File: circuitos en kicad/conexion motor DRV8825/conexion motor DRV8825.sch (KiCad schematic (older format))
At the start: 29 parts, among them P1 CONN_3X2, P10 CONN_2, P2 CONN_2, P3 CONN_2, P4 CONN_2, P5 CONN_2, P6 CONN_2, P7 CONN_2, P8 CONN_2, P9 CONN_2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

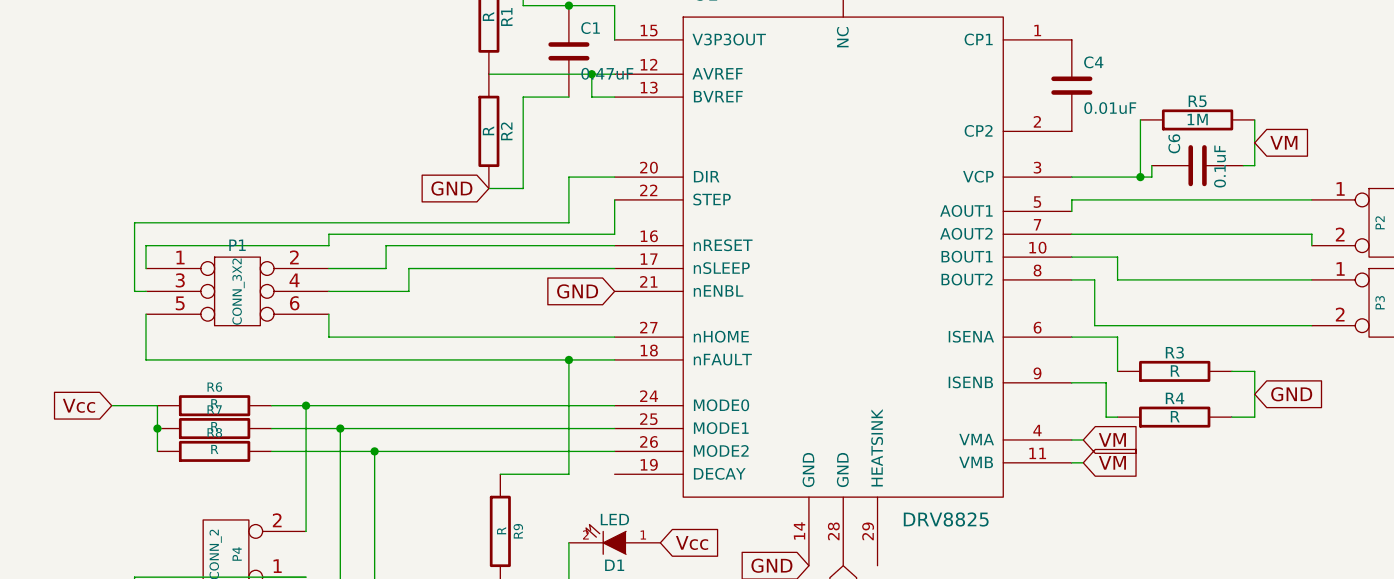
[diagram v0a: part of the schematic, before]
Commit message: Placa del DRV8825 actualizada al 25/07/2014
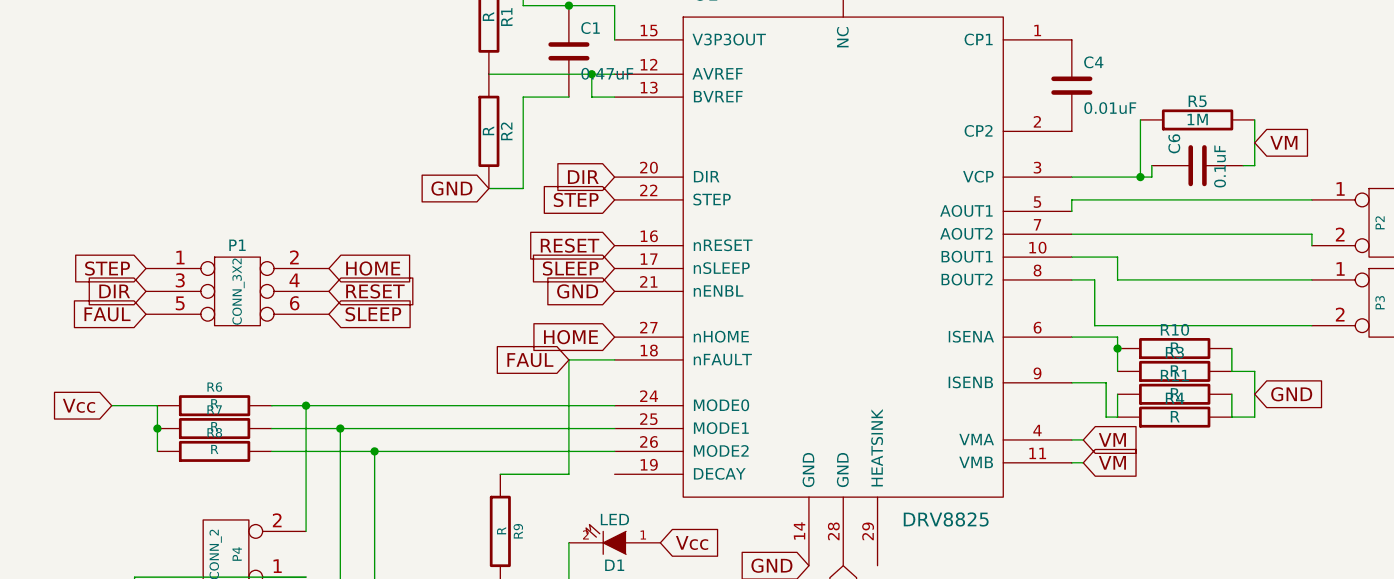
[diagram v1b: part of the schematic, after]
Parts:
- added R10, R11: R, symbol R
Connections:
- net GND: now also R10.2, R11.2
- net at R4.1, U1.9 (ISENB): now also R11.1
- net at R3.1, U1.6 (ISENA): now also R10.1
- net HOME: now reaches P1.2
- net HOME: now also U1.27 (nHOME); no longer U1.16 (nRESET)
- net RESET: now reaches P1.4
- net RESET: now also U1.16 (nRESET); no longer U1.17 (nSLEEP)
- net FAUL: now reaches P1.5, R9.1, U1.18 (nFAULT)
- net DIR: now reaches P1.3, U1.20 (DIR)
- net STEP: now reaches P1.1, U1.22 (STEP)
- net SLEEP: now reaches P1.6
- net SLEEP: now also U1.17 (nSLEEP); no longer U1.27 (nHOME)
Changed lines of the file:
@@
 Sheet 1 1
 Title ""
-Date "25 apr 2014"
+Date "15 jun 2014"
 Rev ""
 Comp ""
@@
 $EndDescr
 Wire Wire Line
-	3350 4050 3700 4050
-Wire Wire Line
-	3700 4050 3700 3950
-Wire Wire Line
-	3700 3950 4600 3950
-Wire Wire Line
-	4600 3800 3350 3800
-Wire Wire Line
-	2500 3750 4400 3750
-Wire Wire Line
 	4950 1900 5500 1900
 Connection ~ 5900 2300
@@
 	5900 2200 5900 2300
 Wire Wire Line
-	2550 4350 4600 4350
-Wire Wire Line
-	4600 3800 4600 3650
-Wire Wire Line
 	7300 4600 7400 4600
 Wire Wire Line
@@
 	7400 4400 7300 4400
 Wire Wire Line
-	6800 4400 6800 4250
+	6800 4250 6800 4400
 Wire Wire Line
 	6800 4250 6600 4250
@@
 Wire Wire Line
 	6750 4600 6800 4600
-Wire Wire Line
-	4600 3550 4400 3550
-Wire Wire Line
-	4400 3550 4400 3750
 Connection ~ 5400 1900
 Connection ~ 6400 1900
 Wire Wire Line
 	5100 2300 6400 2300
-Wire Wire Line
-	3350 3800 3350 3850
-Wire Wire Line
-	4600 3850 3600 3850
-Wire Wire Line
-	3600 3850 3600 3950
-Wire Wire Line
-	3600 3950 3350 3950
-Wire Wire Line
-	4600 4250 3350 4250
-Wire Wire Line
-	3350 4250 3350 4150
 Wire Wire Line
 	4600 3200 4500 3200
@@
 	2600 4550 2600 4750
 Connection ~ 2600 4650
-Wire Wire Line
-	2550 4350 2550 4150
-Connection ~ 4400 4350
 $Comp
 L R R9
@@
 	1    0    0    -1
 $EndComp
-Wire Wire Line
-	3350 3850 2550 3850
-Wire Wire Line
-	2550 3850 2550 3950
-Wire Wire Line
-	2500 3750 2500 4050
-Wire Wire Line
-	2500 4050 2550 4050
 Text GLabel 6650 4800 2    60   Input ~ 0
 VM
@@
 	6650 1900 6950 1900
 Connection ~ 6950 1900
+$Comp
+L R R10
+U 1 1 539DBE41
+P 7050 4300
+F 0 "R10" V 7130 4300 50  0000 C CNN
+F 1 "R" V 7050 4300 50  0000 C CNN
+F 2 "" H 7050 4300 60  0001 C CNN
+F 3 "" H 7050 4300 60  0001 C CNN
+	1    7050 4300
+	0    -1   -1   0
+$EndComp
+$Comp
+L R R11
+U 1 1 539DBE47
+P 7050 4500
+F 0 "R11" V 7130 4500 50  0000 C CNN
+F 1 "R" V 7050 4500 50  0000 C CNN
+F 2 "" H 7050 4500 60  0001 C CNN
+F 3 "" H 7050 4500 60  0001 C CNN
+	1    7050 4500
+	0    -1   -1   0
+$EndComp
+Wire Wire Line
+	6800 4600 6800 4500
+Wire Wire Line
+	7300 4500 7300 4600
+Wire Wire Line
+	7300 4400 7300 4300
+Connection ~ 6800 4300
+Text GLabel 2550 3950 0    60   Input ~ 0
+STEP
+Text GLabel 2550 4050 0    60   Input ~ 0
+DIR
+Text GLabel 2550 4150 0    60   Input ~ 0
+FAUL
+Text GLabel 3350 3950 2    60   Input ~ 0
+HOME
+Text GLabel 3350 4150 2    60   Input ~ 0
+SLEEP
+Text GLabel 3350 4050 2    60   Input ~ 0
+RESET
+Wire Wire Line
+	4400 4350 4600 4350
+Text GLabel 4600 3650 0    60   Input ~ 0
+STEP
+Text GLabel 4600 3550 0    60   Input ~ 0
+DIR
+Text GLabel 4400 4350 0    60   Input ~ 0
+FAUL
+Text GLabel 4600 4250 0    60   Input ~ 0
+HOME
+Text GLabel 4600 3950 0    60   Input ~ 0
+SLEEP
+Text GLabel 4600 3850 0    60   Input ~ 0
+RESET
 $EndSCHEMATC
